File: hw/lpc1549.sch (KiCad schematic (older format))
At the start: 19 parts, among them J1001 ARM_JTAG_SWD_HEADER_10_PINSMD, U1001 MCP2551_SOIC8, U1002 LPC1549JBD64, X1001 XTAL_7A-12.000MAAJ-T

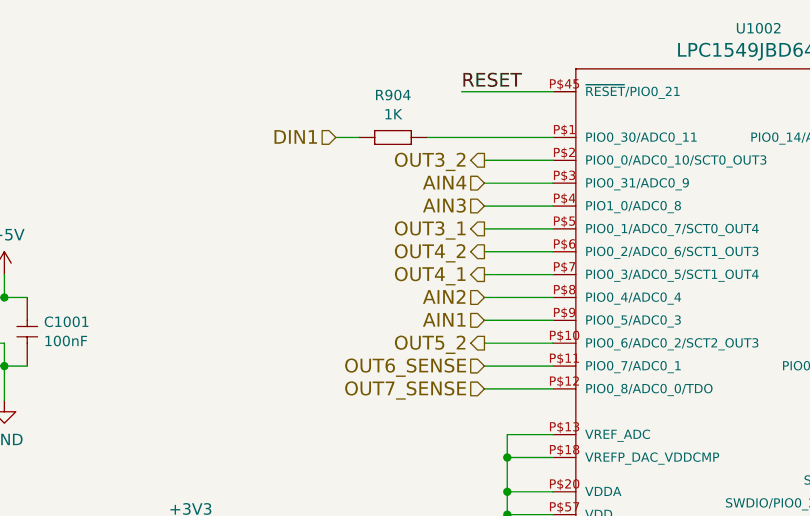
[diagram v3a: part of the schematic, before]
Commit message: analog inputs replaced with digital inputs
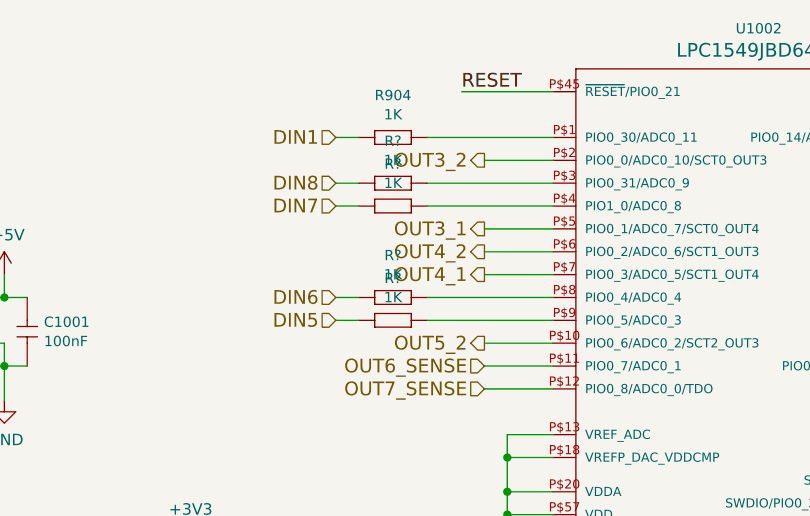
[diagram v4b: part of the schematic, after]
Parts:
- added R? (x4): 1K, yageo:0603, symbol icu-rescue:1K
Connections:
- net AIN1: no longer names the net of U1002.P$9 (PIO0_5/ADC0_3)
- net AIN1: now also R?.1 (R1)
- net AIN2: no longer names the net of U1002.P$8 (PIO0_4/ADC0_4)
- net AIN2: now also R?.1 (R1)
- net AIN3: no longer names the net of U1002.P$4 (PIO1_0/ADC0_8)
- net AIN3: now also R?.1 (R1)
- net AIN4: no longer names the net of U1002.P$3 (PIO0_31/ADC0_9)
- net AIN4: now also R?.1 (R1)
- new net DIN5: R?.2 (R2)
- new net DIN6: R?.2 (R2)
- new net DIN7: R?.2 (R2)
- new net DIN8: R?.2 (R2)
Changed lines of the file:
@@
 $Descr A4 11693 8268
 encoding utf-8
-Sheet 9 14
+Sheet 9 10
 Title ""
 Date ""
@@
 	7850 5550 7950 5550
 Wire Wire Line
-	5200 2950 4900 2950
-Text HLabel 4900 2950 0    60   Input ~ 0
-AIN1
-Wire Wire Line
-	5200 2850 4900 2850
-Text HLabel 4900 2850 0    60   Input ~ 0
-AIN2
-Wire Wire Line
-	5200 2450 4900 2450
-Text HLabel 4900 2450 0    60   Input ~ 0
-AIN3
-Wire Wire Line
-	5200 2350 4900 2350
-Text HLabel 4900 2350 0    60   Input ~ 0
-AIN4
+	5200 2950 4650 2950
+Text HLabel 4250 2950 0    60   Input ~ 0
+DIN5
+Wire Wire Line
+	5200 2850 4650 2850
+Text HLabel 4250 2850 0    60   Input ~ 0
+DIN6
+Wire Wire Line
+	5200 2450 4650 2450
+Text HLabel 4250 2450 0    60   Input ~ 0
+DIN7
+Wire Wire Line
+	5200 2350 4650 2350
+Text HLabel 4250 2350 0    60   Input ~ 0
+DIN8
 Text HLabel 8300 4750 2    60   Input ~ 0
 DIN4
@@
 Wire Wire Line
 	3600 4100 3950 4100
+$Comp
+L icu-rescue:1K R?
+U 1 1 5B1F4296
+P 4450 2350
+F 0 "R?" H 4500 2534 45  0000 C CNN
+F 1 "1K" H 4500 2450 45  0000 C CNN
+F 2 "yageo:0603" H 4480 2500 20  0001 C CNN
+F 3 "" H 4419 2389 60  0001 C CNN
+F 4 "" H 4819 2789 60  0001 C CNN "1st Source Part Number"
+F 5 "Digikey" H 4719 2689 60  0001 C CNN "1st Source"
+F 6 "RC0603FR-071KL" H 4619 2589 60  0001 C CNN "Manufacturer Part Number"
+F 7 "YAGEO" H 4519 2489 60  0001 C CNN "Manufacturer"
+	1    4450 2350
+	1    0    0    -1
+$EndComp
+$Comp
+L icu-rescue:1K R?
+U 1 1 5B1F42DA
+P 4450 2450
+F 0 "R?" H 4500 2634 45  0000 C CNN
+F 1 "1K" H 4500 2550 45  0000 C CNN
+F 2 "yageo:0603" H 4480 2600 20  0001 C CNN
+F 3 "" H 4419 2489 60  0001 C CNN
+F 4 "" H 4819 2889 60  0001 C CNN "1st Source Part Number"
+F 5 "Digikey" H 4719 2789 60  0001 C CNN "1st Source"
+F 6 "RC0603FR-071KL" H 4619 2689 60  0001 C CNN "Manufacturer Part Number"
+F 7 "YAGEO" H 4519 2589 60  0001 C CNN "Manufacturer"
+	1    4450 2450
+	1    0    0    -1
+$EndComp
+$Comp
+L icu-rescue:1K R?
+U 1 1 5B1F431C
+P 4450 2850
+F 0 "R?" H 4500 3034 45  0000 C CNN
+F 1 "1K" H 4500 2950 45  0000 C CNN
+F 2 "yageo:0603" H 4480 3000 20  0001 C CNN
+F 3 "" H 4419 2889 60  0001 C CNN
+F 4 "" H 4819 3289 60  0001 C CNN "1st Source Part Number"
+F 5 "Digikey" H 4719 3189 60  0001 C CNN "1st Source"
+F 6 "RC0603FR-071KL" H 4619 3089 60  0001 C CNN "Manufacturer Part Number"
+F 7 "YAGEO" H 4519 2989 60  0001 C CNN "Manufacturer"
+	1    4450 2850
+	1    0    0    -1
+$EndComp
+$Comp
+L icu-rescue:1K R?
+U 1 1 5B1F436C
+P 4450 2950
+F 0 "R?" H 4500 3134 45  0000 C CNN
+F 1 "1K" H 4500 3050 45  0000 C CNN
+F 2 "yageo:0603" H 4480 3100 20  0001 C CNN
+F 3 "" H 4419 2989 60  0001 C CNN
+F 4 "" H 4819 3389 60  0001 C CNN "1st Source Part Number"
+F 5 "Digikey" H 4719 3289 60  0001 C CNN "1st Source"
+F 6 "RC0603FR-071KL" H 4619 3189 60  0001 C CNN "Manufacturer Part Number"
+F 7 "YAGEO" H 4519 3089 60  0001 C CNN "Manufacturer"
+	1    4450 2950
+	1    0    0    -1
+$EndComp
+Wire Wire Line
+	4350 2950 4250 2950
+Wire Wire Line
+	4250 2850 4350 2850
+Wire Wire Line
+	4350 2450 4250 2450
+Wire Wire Line
+	4350 2350 4250 2350
 $EndSCHEMATC

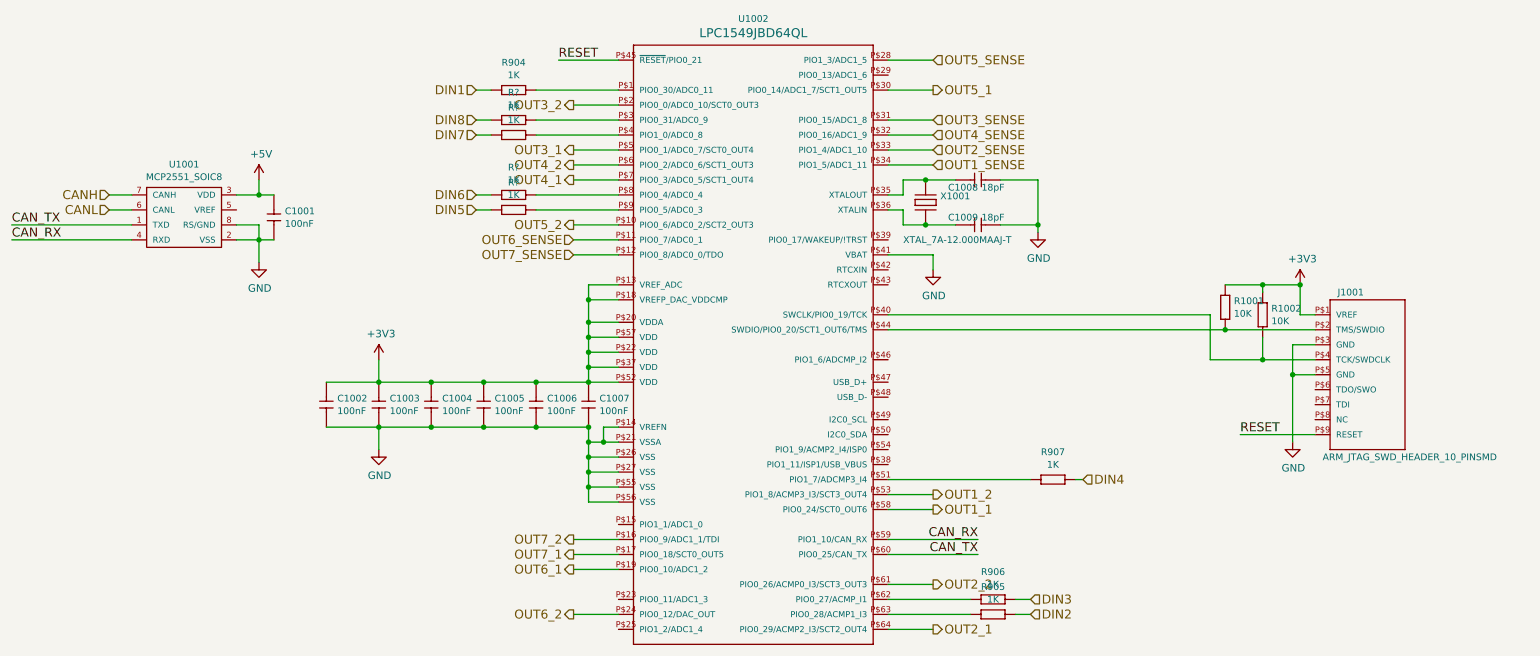
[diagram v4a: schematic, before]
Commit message: pcb 2.0 created, with imu
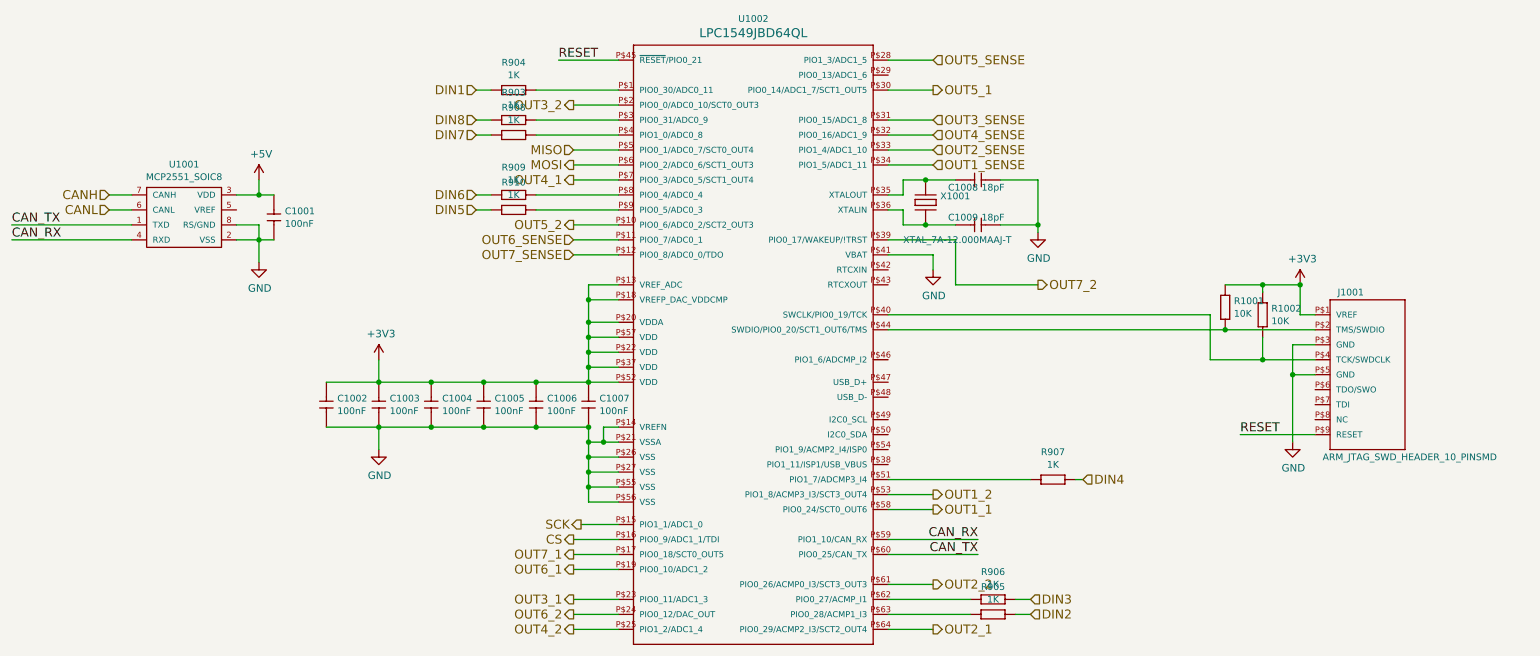
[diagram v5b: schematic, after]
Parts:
- gave numbers to parts that had none: 4
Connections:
- net OUT3_1: now also U1002.P$23 (PIO0_11/ADC1_3); no longer U1002.P$5 (PIO0_1/ADC0_7/SCT0_OUT4)
- net OUT4_2: now also U1002.P$25 (PIO1_2/ADC1_4); no longer U1002.P$6 (PIO0_2/ADC0_6/SCT1_OUT3)
- net OUT7_2: now also U1002.P$39 (PIO0_17/WAKEUP/!TRST); no longer U1002.P$16 (PIO0_9/ADC1_1/TDI)
- net SCK: now reaches U1002.P$15 (PIO1_1/ADC1_0)
- new net CS: U1002.P$16 (PIO0_9/ADC1_1/TDI)
- new net MISO: U1002.P$5 (PIO0_1/ADC0_7/SCT0_OUT4)
- new net MOSI: U1002.P$6 (PIO0_2/ADC0_6/SCT1_OUT3)
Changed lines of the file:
@@
 $Descr A4 11693 8268
 encoding utf-8
-Sheet 9 10
+Sheet 9 11
 Title ""
 Date ""
@@
 OUT2_2
 Wire Wire Line
-	5200 2550 4900 2550
-Text HLabel 4900 2550 0    60   Output ~ 0
+	5200 5550 4900 5550
+Text HLabel 4900 5550 0    60   Output ~ 0
 OUT3_1
 Wire Wire Line
@@
 OUT4_1
 Wire Wire Line
-	5200 2650 4900 2650
-Text HLabel 4900 2650 0    60   Output ~ 0
+	5200 5750 4900 5750
+Text HLabel 4900 5750 0    60   Output ~ 0
 OUT4_2
 Wire Wire Line
@@
 Text HLabel 4900 5250 0    60   Output ~ 0
 OUT7_1
-Wire Wire Line
-	5200 5150 4900 5150
-Text HLabel 4900 5150 0    60   Output ~ 0
+Text HLabel 8000 3450 2    60   Output ~ 0
 OUT7_2
 Wire Wire Line
@@
 	3600 4100 3950 4100
 $Comp
-L icu-rescue:1K R?
+L icu-rescue:1K R903
 U 1 1 5B1F4296
 P 4450 2350
-F 0 "R?" H 4500 2534 45  0000 C CNN
+F 0 "R903" H 4500 2534 45  0000 C CNN
 F 1 "1K" H 4500 2450 45  0000 C CNN
 F 2 "yageo:0603" H 4480 2500 20  0001 C CNN
@@
 $EndComp
 $Comp
-L icu-rescue:1K R?
+L icu-rescue:1K R908
 U 1 1 5B1F42DA
 P 4450 2450
-F 0 "R?" H 4500 2634 45  0000 C CNN
+F 0 "R908" H 4500 2634 45  0000 C CNN
 F 1 "1K" H 4500 2550 45  0000 C CNN
 F 2 "yageo:0603" H 4480 2600 20  0001 C CNN
@@
 $EndComp
 $Comp
-L icu-rescue:1K R?
+L icu-rescue:1K R909
 U 1 1 5B1F431C
 P 4450 2850
-F 0 "R?" H 4500 3034 45  0000 C CNN
+F 0 "R909" H 4500 3034 45  0000 C CNN
 F 1 "1K" H 4500 2950 45  0000 C CNN
 F 2 "yageo:0603" H 4480 3000 20  0001 C CNN
@@
 $EndComp
 $Comp
-L icu-rescue:1K R?
+L icu-rescue:1K R910
 U 1 1 5B1F436C
 P 4450 2950
-F 0 "R?" H 4500 3134 45  0000 C CNN
+F 0 "R910" H 4500 3134 45  0000 C CNN
 F 1 "1K" H 4500 3050 45  0000 C CNN
 F 2 "yageo:0603" H 4480 3100 20  0001 C CNN
@@
 Wire Wire Line
 	4350 2350 4250 2350
+Wire Wire Line
+	5200 2650 4900 2650
+Wire Wire Line
+	4900 2550 5200 2550
+Text HLabel 4900 2650 0    60   Output ~ 0
+MOSI
+Text HLabel 4900 2550 0    60   Input ~ 0
+MISO
+Wire Wire Line
+	5200 5150 4900 5150
+Text HLabel 4900 5150 0    60   Output ~ 0
+CS
+Wire Wire Line
+	5200 5050 4950 5050
+Text HLabel 4950 5050 0    60   Output ~ 0
+SCK
+Wire Wire Line
+	7450 3450 7450 3150
+Wire Wire Line
+	7450 3150 7000 3150
+Wire Wire Line
+	7450 3450 8000 3450
 $EndSCHEMATC
